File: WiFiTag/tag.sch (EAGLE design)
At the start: 65 parts, among them IC2 MCP73831/OT, U2 CP2104-F03-GM

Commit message: WifiTagV0.4
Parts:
- removed C4: 10uF, microbuilder:CAP_CERAMIC0603
- removed D2: (no value), adafruit:DIODESOD-123
- removed EN, VBUS: (no value), wirepad:SMD2
- removed LED2: RED, microbuilder:LED0603
- removed LED3: GREEN, microbuilder:LED0603
- removed R8, R9: 10k, microbuilder:RESISTOR0402
- removed T1, T2: (no value), transistor:MMBT2222ALT1-NPN-SOT23-BEC
- removed U2: CP2104-F03-GM, Silicon Labs:CP2104-F03-GM
- removed U3: (no value), MicroUSB:USB""
- added GND1, SET: (no value), wirepad:SMD2
- added JP1, JP2: (no value), pinhead:PINHD-1X55X2MM
- R4, R5: value 1k -> 10k
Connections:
- removed net D+: U2.D+, U3.D+
- removed net D-: U2.D-, U3.D-
- removed net DTR: R8.1, T2.E, U2.DTR
- removed net N$10: R8.2, T1.B
- removed net N$11: R9.2, T2.B
- removed net N$6: LED2.A, R4.2
- removed net N$7: LED3.A, R5.2
- removed net N$8: LED2.C, U2.GPIO0
- removed net N$9: LED3.C, U2.GPIO1
- removed net RTS: R9.1, T1.E, U2.RTS
- removed net VBUS: C4.P$1, D2.A, U2.REGIN, U2.VBUS, U3.VBUS, VBUS.P
- net 0: now also JP1.1, R4.1; no longer R18.1, T2.C
- net 2: now also R18.1
- net 3.3V: now also JP2.4, R4.2, R5.2, U$24.EN
- net 5.0V: now also JP2.5; no longer D2.C
- net EN: now also JP1.5; no longer EN.P
- net GND: now also GND1.P, JP2.1; no longer C4.P$2, U2.GND, U3.GND
- net RST: now also JP1.2, R5.1; no longer T1.C
- net RXD: now also JP1.3; no longer U2.RXD
- net SETLATCH: now also SET.P; no longer R4.1, R5.1, U2.VDD, U2.VIO
- net TXD: now also JP1.4; no longer U2.TXD
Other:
- moved on the sheet: R4, R5

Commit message: new tag version 0.5
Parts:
- removed JP1, JP2: (no value), pinhead:PINHD-1X55X2MM
- removed U$21, U$47, U$48, U$49: MOUNTINGHOLE2.5, microbuilder:MOUNTINGHOLE2.5
- removed U$24: CD4043B, masterthesis:CD4043B
- added 16, BAT1, EN: (no value), wirepad:SMD2
- added Q1: (no value), microbuilder:TRANSISTOR_PNPSOT23-REFLOW
- added R8: 10k, microbuilder:RESISTOR0402
- R20: value 150 -> 10k
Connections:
- removed net BATLOW: R10.1, U$24.Q2
- removed net RESETLATCH: U$24.R1, U4.Y
- removed net SETLATCH: SET.P, U$24.S1, U5.INT1
- new net N$6: Q1.C, R8.2, U4.A
- new net SET: Q1.E, SET.P, U5.INT1
- net 0: no longer JP1.1
- net 12: no longer U$24.S2
- net 14: now also R10.1; no longer U$24.R2
- net 16: now also 16.P, Q1.B; no longer U4.A
- net 2: now also LED6.C; no longer R18.1
- net 3.3V: now also R18.2, U5.CS; no longer JP2.4, U$24.EN, U$24.VCC
- net 4.5V: now also BAT1.P
- net 5.0V: no longer JP2.5
- net EN: now also EN.P, U4.Y; no longer JP1.5, U$24.Q1
- net GND: now also R8.1, U5.GND@2; no longer JP2.1, LED6.C, U$24.GND
- net N$4: now also R18.1; no longer R18.2
- net RST: no longer JP1.2
- net RXD: no longer JP1.3
- net TXD: no longer JP1.4
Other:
- moved on the sheet: 3.3V, 5V, GND1, LED6, R18, R19, R20, SET, U4, U5

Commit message: XNOR Tag version
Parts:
- removed Q1: (no value), microbuilder:TRANSISTOR_PNPSOT23-REFLOW
- removed R8: 10k, microbuilder:RESISTOR0402
- removed U4: (no value), microbuilder:74LVC1G04
- added C14: 470nF, microbuilder:CAP_CERAMIC0402
- added C4: 10nF, microbuilder:CAP_CERAMIC0402
- added R21, R22, R23, R9: 10k, microbuilder:RESISTOR0402
- added R24, R25: 100k, microbuilder:RESISTOR0402
- added U$46: CD4077B, masterthesis:CD4077B
- R1: value (none) -> 1k
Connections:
- removed net N$6: Q1.C, R8.2, U4.A
- new net N$10: R25.1, U$46.A
- new net N$7: R9.1, U5.SDO
- new net N$8: R21.2, U5.CS
- new net N$9: R20.2, U$46.~G#H
- net 12: now also R11.1
- net 13: no longer R11.1
- net 16: now also U$46.B, U$46.G; no longer Q1.B
- net 3.3V: now also C14.P$1, C4.P$2, R21.1, R22.2, R23.1, R24.2, R25.2, U$46.VCC; no longer R20.1, U4.VCC, U5.CS
- net 4: now also R22.1
- net 5: now also R23.2
- net EN: now also R20.1, R24.1, U$46.~A#B; no longer R20.2, U4.Y
- net GND: now also C14.P$2, C4.P$1, R9.2, U$46.GND; no longer R8.1, U4.GND
- net SET: now also U$46.H; no longer Q1.E
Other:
- moved on the sheet: R20

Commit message: XNOR Tag version
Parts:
- removed AC1, AC2, BAT1, GND1: (no value), wirepad:SMD2
- removed C14: 470nF, microbuilder:CAP_CERAMIC0402
- removed C4: 10nF, microbuilder:CAP_CERAMIC0402
- removed R21, R22, R23, R9: 10k, microbuilder:RESISTOR0402
- removed U5: (no value), microbuilder:ACCEL_LIS3DHTR
- added C17: 1uF, microbuilder:CAP_CERAMIC0402
- added C18: 100nf, microbuilder:CAP_CERAMIC0402
- added JP1, JP2: (no value), microbuilder:HEADER-1X2
- added Q3, Q4: BSS138, microbuilder:MOSFET-NWIDE
- added R31, R32, R33, R34, R35, R36: 10K, microbuilder:RESISTOR0402
- added U3: LIS3DHTR, microbuilder:ACCEL_LIS3DHTR
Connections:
- removed net 4: R22.1, U5.SDA, X1.GPIO4
- removed net 5: R23.2, U5.SCL, X1.GPIO5
- removed net N$7: R9.1, U5.SDO
- removed net N$8: R21.2, U5.CS
- new net ADC1: U3.ADC1
- new net ADC2: U3.ADC2
- new net ADC3: U3.ADC3
- new net N$11: R31.1, U3.CS
- new net SCL: Q4.D, R35.1, X1.GPIO5
- new net SCL_3.3V: Q4.S, R33.1, U3.SCL
- new net SDA: Q3.D, R34.1, X1.GPIO4
- new net SDA_3.3V: Q3.S, R32.1, U3.SDA
- new net SDO: R36.2, U3.SDO
- net 3.3V: now also C17.P$1, C18.P$1, Q3.G, Q4.G, R31.2, R32.2, R33.2, R34.2, R35.2, U3.VDD, U3.VDDIO; no longer C14.P$1, C4.P$2, R21.1, R22.2, R23.1, U5.VDD, U5.VDDIO
- net 4.5V: now also JP1.1; no longer BAT1.P
- net AC1: now also JP2.1; no longer AC1.P
- net AC2: now also JP2.2; no longer AC2.P
- net GND: now also C17.P$2, C18.P$2, JP1.2, R36.1, U3.GND@1, U3.GND@2, U3.RES(GND); no longer C14.P$2, C4.P$1, GND1.P, R9.2, U5.GND@1, U5.GND@2, U5.RES(GND)
- net SET: now also U3.INT1; no longer U5.INT1
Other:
- note added: "Set SJ1 to make I2C"
- note added: "address LSB 1"
- moved on the sheet: BAT, C10, C11, C12, C13, C6, C7, C8, C9, GND, R14, R15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

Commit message: V06 of PCB
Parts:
- removed R20: 10k, microbuilder:RESISTOR0402
- removed R25: 100k, microbuilder:RESISTOR0402
- removed U$46: CD4077B, masterthesis:CD4077B
- added U2: (no value), microbuilder:74LVC1G04
- R24: value 100k -> 10k
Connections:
- removed net N$10: R25.1, U$46.A
- removed net N$9: R20.2, U$46.~G#H
- net 16: no longer U$46.B, U$46.G
- net 3.3V: now also U2.VCC; no longer R25.2, U$46.VCC
- net EN: no longer R20.1, U$46.~A#B
- net GND: now also U2.GND; no longer U$46.GND
- net RST: now also U2.Y
- net SET: now also U2.A; no longer U$46.H
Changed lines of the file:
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@@
 <part name="U$23" library="microbuilder" deviceset="GND" device=""/>
 <part name="U$22" library="microbuilder" deviceset="4.5V" device=""/>
-<part name="U$26" library="microbuilder" deviceset="3.3V" device=""/>
 <part name="U$31" library="microbuilder" deviceset="GND" device=""/>
 <part name="U$32" library="microbuilder" deviceset="GND" device=""/>
@@
 <part name="LED6" library="microbuilder" deviceset="LED" device="0603" value="BLUE"/>
 <part name="R19" library="microbuilder" deviceset="RESISTOR" device="0402" value="150"/>
-<part name="R20" library="microbuilder" deviceset="RESISTOR" device="0402" value="10k"/>
 <part name="R4" library="microbuilder" deviceset="RESISTOR" device="0402" value="10k"/>
 <part name="U$54" library="microbuilder" deviceset="3.3V" device=""/>
@@
 <part name="U$11" library="microbuilder" deviceset="4.5V" device=""/>
 <part name="U$14" library="microbuilder" deviceset="GND" device=""/>
-<part name="R24" library="microbuilder" deviceset="RESISTOR" device="0402" value="100k"/>
+<part name="R24" library="microbuilder" deviceset="RESISTOR" device="0402" value="10k"/>
 <part name="U$45" library="microbuilder" deviceset="3.3V" device=""/>
-<part name="U$46" library="masterthesis" deviceset="CD4077B" device=""/>
-<part name="U$47" library="microbuilder" deviceset="GND" device=""/>
-<part name="R25" library="microbuilder" deviceset="RESISTOR" device="0402" value="100k"/>
-<part name="U$48" library="microbuilder" deviceset="3.3V" device=""/>
 <part name="U3" library="microbuilder" deviceset="ACCEL_LIS3DHTR" device="" value="LIS3DHTR"/>
 <part name="U$62" library="microbuilder" deviceset="GND" device=""/>
@@
 <part name="JP1" library="microbuilder" deviceset="HEADER-1X2" device=""/>
 <part name="JP2" library="microbuilder" deviceset="HEADER-1X2" device=""/>
+<part name="U2" library="microbuilder" deviceset="74LVC1G04" device=""/>
+<part name="U$24" library="microbuilder" deviceset="3.3V" device=""/>
+<part name="U$25" library="microbuilder" deviceset="GND" device=""/>
 </parts>
 <sheets>
@@
 <instance part="U$23" gate="G$1" x="111.76" y="17.78"/>
 <instance part="U$22" gate="G$1" x="111.76" y="30.48"/>
-<instance part="U$26" gate="G$1" x="-83.82" y="-35.56"/>
 <instance part="U$31" gate="G$1" x="121.92" y="-22.86"/>
 <instance part="U$32" gate="G$1" x="116.84" y="-22.86"/>
@@
 <instance part="LED6" gate="G$1" x="78.74" y="12.7" rot="R180"/>
 <instance part="R19" gate="G$1" x="10.16" y="40.64" rot="R180"/>
-<instance part="R20" gate="G$1" x="-76.2" y="-40.64" rot="R270"/>
 <instance part="R4" gate="G$1" x="40.64" y="15.24" rot="R90"/>
 <instance part="U$54" gate="G$1" x="40.64" y="22.86"/>
@@
 <instance part="R24" gate="G$1" x="-15.24" y="20.32" rot="R90"/>
 <instance part="U$45" gate="G$1" x="-15.24" y="27.94"/>
-<instance part="U$46" gate="G$1" x="-96.52" y="-45.72"/>
-<instance part="U$47" gate="G$1" x="-109.22" y="-55.88"/>
-<instance part="R25" gate="G$1" x="-114.3" y="-38.1" rot="R180"/>
-<instance part="U$48" gate="G$1" x="-119.38" y="-35.56"/>
 <instance part="U3" gate="G$1" x="30.48" y="-109.22"/>
 <instance part="U$62" gate="G$1" x="12.7" y="-119.38"/>
@@
 <instance part="JP1" gate="G$1" x="-45.72" y="43.18"/>
 <instance part="JP2" gate="G$1" x="165.1" y="-27.94"/>
+<instance part="U2" gate="G$1" x="-71.12" y="-50.8"/>
+<instance part="U$24" gate="G$1" x="-60.96" y="-43.18"/>
+<instance part="U$25" gate="G$1" x="-81.28" y="-58.42"/>
 </instances>
 <busses>
@@
 </segment>
 <segment>
-<pinref part="U$46" gate="G$1" pin="GND"/>
-<pinref part="U$47" gate="G$1" pin="GND"/>
-</segment>
-<segment>
 <pinref part="U3" gate="G$1" pin="GND@1"/>
 <pinref part="U$62" gate="G$1" pin="GND"/>
@@
 <wire x1="-55.88" y1="43.18" x2="-48.26" y2="43.18" width="0.1524" layer="91"/>
 </segment>
+<segment>
+<pinref part="U2" gate="G$1" pin="GND"/>
+<pinref part="U$25" gate="G$1" pin="GND"/>
+</segment>
 </net>
 <net name="3.3V" class="0">
@@
 <pinref part="R24" gate="G$1" pin="2"/>
 <pinref part="U$45" gate="G$1" pin="3.3V"/>
-</segment>
-<segment>
-<pinref part="U$46" gate="G$1" pin="VCC"/>
-<pinref part="U$26" gate="G$1" pin="3.3V"/>
-</segment>
-<segment>
-<pinref part="R25" gate="G$1" pin="2"/>
-<pinref part="U$48" gate="G$1" pin="3.3V"/>
 </segment>
 <segment>
@@
 <pinref part="U$21" gate="G$1" pin="3.3V"/>
 </segment>
+<segment>
+<pinref part="U2" gate="G$1" pin="VCC"/>
+<pinref part="U$24" gate="G$1" pin="3.3V"/>
+</segment>
 </net>
 <net name="N$5" class="0">
@@
 </segment>
 <segment>
-<pinref part="U$46" gate="G$1" pin="H"/>
-<wire x1="-83.82" y1="-40.64" x2="-81.28" y2="-40.64" width="0.1524" layer="91"/>
-<label x="-83.82" y="-40.64" size="1.778" layer="95"/>
-</segment>
-<segment>
 <pinref part="U3" gate="G$1" pin="INT1"/>
 <wire x1="45.72" y1="-109.22" x2="53.34" y2="-109.22" width="0.1524" layer="91"/>
 <label x="48.26" y="-109.22" size="1.778" layer="95"/>
+</segment>
+<segment>
+<pinref part="U2" gate="G$1" pin="A"/>
+<wire x1="-81.28" y1="-50.8" x2="-86.36" y2="-50.8" width="0.1524" layer="91"/>
+<label x="-86.36" y="-50.8" size="1.778" layer="95"/>
 </segment>
 </net>
@@
 <label x="15.24" y="40.64" size="1.778" layer="95"/>
 <pinref part="R19" gate="G$1" pin="1"/>
+</segment>
+<segment>
+<pinref part="U2" gate="G$1" pin="Y"/>
+<wire x1="-60.96" y1="-55.88" x2="-55.88" y2="-55.88" width="0.1524" layer="91"/>
+<label x="-60.96" y="-55.88" size="1.778" layer="95"/>
 </segment>
 </net>
@@
 <label x="-10.16" y="76.2" size="1.778" layer="95"/>
 </segment>
-<segment>
-<pinref part="R20" gate="G$1" pin="1"/>
-<wire x1="-76.2" y1="-35.56" x2="-76.2" y2="-33.02" width="0.1524" layer="91"/>
-<label x="-76.2" y="-35.56" size="1.778" layer="95" rot="R90"/>
-</segment>
-<segment>
-<pinref part="U$46" gate="G$1" pin="~A#B"/>
-<wire x1="-109.22" y1="-43.18" x2="-114.3" y2="-43.18" width="0.1524" layer="91"/>
-<label x="-114.3" y="-43.18" size="1.778" layer="95"/>
-</segment>
 </net>
 <net name="16" class="0">
@@
 <wire x1="-10.16" y1="68.58" x2="-5.08" y2="68.58" width="0.1524" layer="91"/>
 <label x="-10.16" y="68.58" size="1.778" layer="95"/>
-</segment>
-<segment>
-<pinref part="U$46" gate="G$1" pin="G"/>
-<wire x1="-83.82" y1="-43.18" x2="-81.28" y2="-43.18" width="0.1524" layer="91"/>
-<label x="-83.82" y="-43.18" size="1.778" layer="95"/>
-</segment>
-<segment>
-<pinref part="U$46" gate="G$1" pin="B"/>
-<wire x1="-109.22" y1="-40.64" x2="-111.76" y2="-40.64" width="0.1524" layer="91"/>
-<label x="-111.76" y="-40.64" size="1.778" layer="95"/>
 </segment>
 </net>
@@
 </segment>
 </net>
-<net name="N$9" class="0">
-<segment>
-<pinref part="U$46" gate="G$1" pin="~G#H"/>
-<pinref part="R20" gate="G$1" pin="2"/>
-<wire x1="-76.2" y1="-45.72" x2="-83.82" y2="-45.72" width="0.1524" layer="91"/>
-</segment>
-</net>
-<net name="N$10" class="0">
-<segment>
-<pinref part="U$46" gate="G$1" pin="A"/>
-<pinref part="R25" gate="G$1" pin="1"/>
-</segment>
-</net>

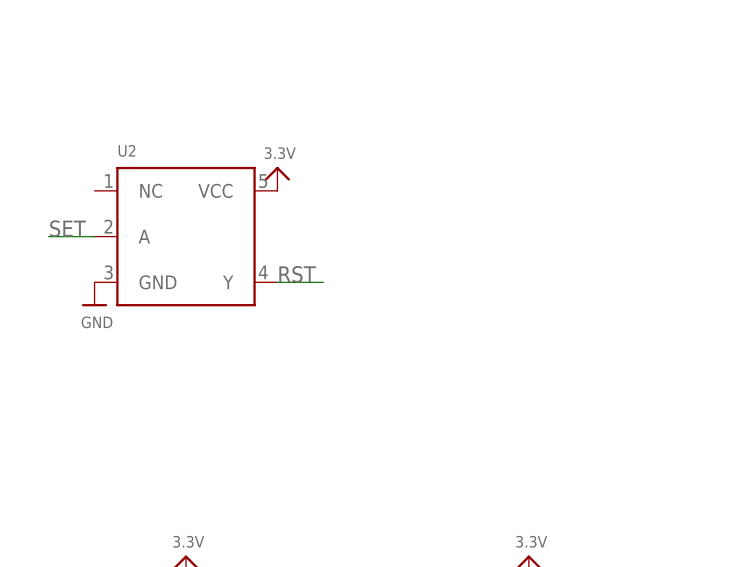
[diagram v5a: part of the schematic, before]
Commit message: Saving current wifitag state
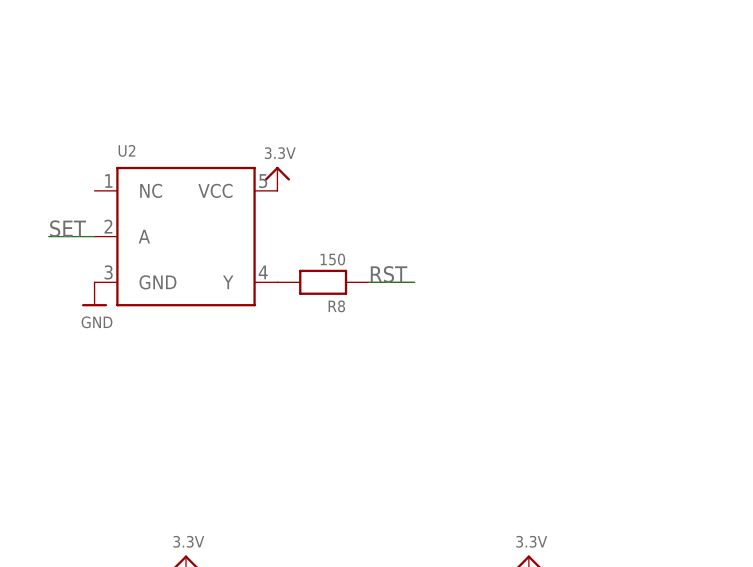
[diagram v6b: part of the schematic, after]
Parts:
- added R8: 150, microbuilder:RESISTOR0402
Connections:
- new net N$6: R8.2, U2.Y
- net RST: now also R8.1; no longer U2.Y
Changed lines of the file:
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@@
 <part name="U$24" library="microbuilder" deviceset="3.3V" device=""/>
 <part name="U$25" library="microbuilder" deviceset="GND" device=""/>
+<part name="R8" library="microbuilder" deviceset="RESISTOR" device="0402" value="150"/>
 </parts>
 <sheets>
@@
 <instance part="U$24" gate="G$1" x="-60.96" y="-43.18"/>
 <instance part="U$25" gate="G$1" x="-81.28" y="-58.42"/>
+<instance part="R8" gate="G$1" x="-55.88" y="-55.88" rot="R180"/>
 </instances>
 <busses>
@@
 </segment>
 <segment>
-<pinref part="U2" gate="G$1" pin="Y"/>
-<wire x1="-60.96" y1="-55.88" x2="-55.88" y2="-55.88" width="0.1524" layer="91"/>
-<label x="-60.96" y="-55.88" size="1.778" layer="95"/>
+<pinref part="R8" gate="G$1" pin="1"/>
+<wire x1="-50.8" y1="-55.88" x2="-45.72" y2="-55.88" width="0.1524" layer="91"/>
+<label x="-50.8" y="-55.88" size="1.778" layer="95"/>
 </segment>
 </net>
@@
 </segment>
 </net>
+<net name="N$6" class="0">
+<segment>
+<pinref part="U2" gate="G$1" pin="Y"/>
+<pinref part="R8" gate="G$1" pin="2"/>
+</segment>
+</net>
